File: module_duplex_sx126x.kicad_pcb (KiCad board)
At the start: 4 copper layers, 55.4 x 49.7 mm, 39 parts, among them J1 USB_B_Mini, J2 Conn_01x06_Pin, J3 Conn_01x05, J4 Conn_01x04, J6 Conn_01x02, SW1 SW_Push, U1 STM32F103C8Tx, U2 AMS1117-3.3, U3 SN65HVD230, U4 Ai-Thinker-Ra-02, U5 Ai-Thinker-Ra-02, Y1 16M, Y2 32.768k

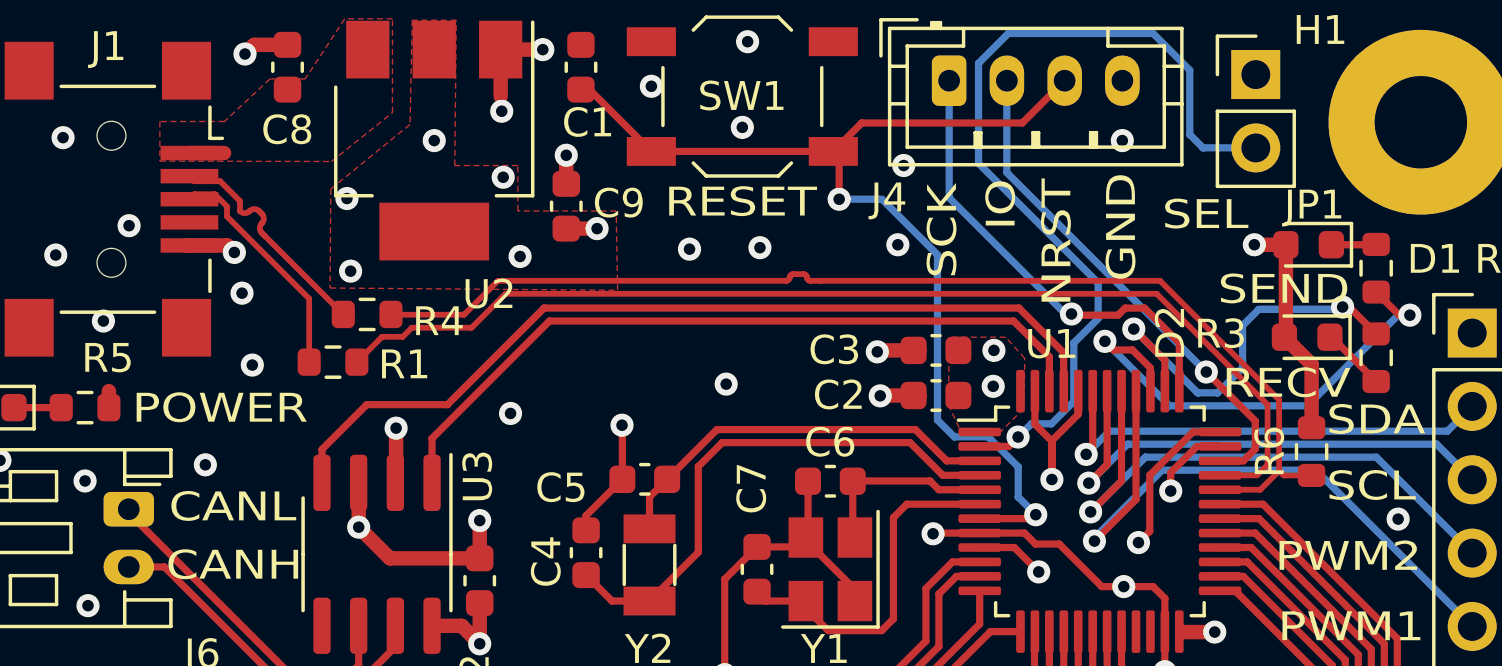
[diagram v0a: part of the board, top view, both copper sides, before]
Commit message: Moved pull up to correct USB_DP
Signed-off-by: Leonardo Celente <leocelente@gmail.com>
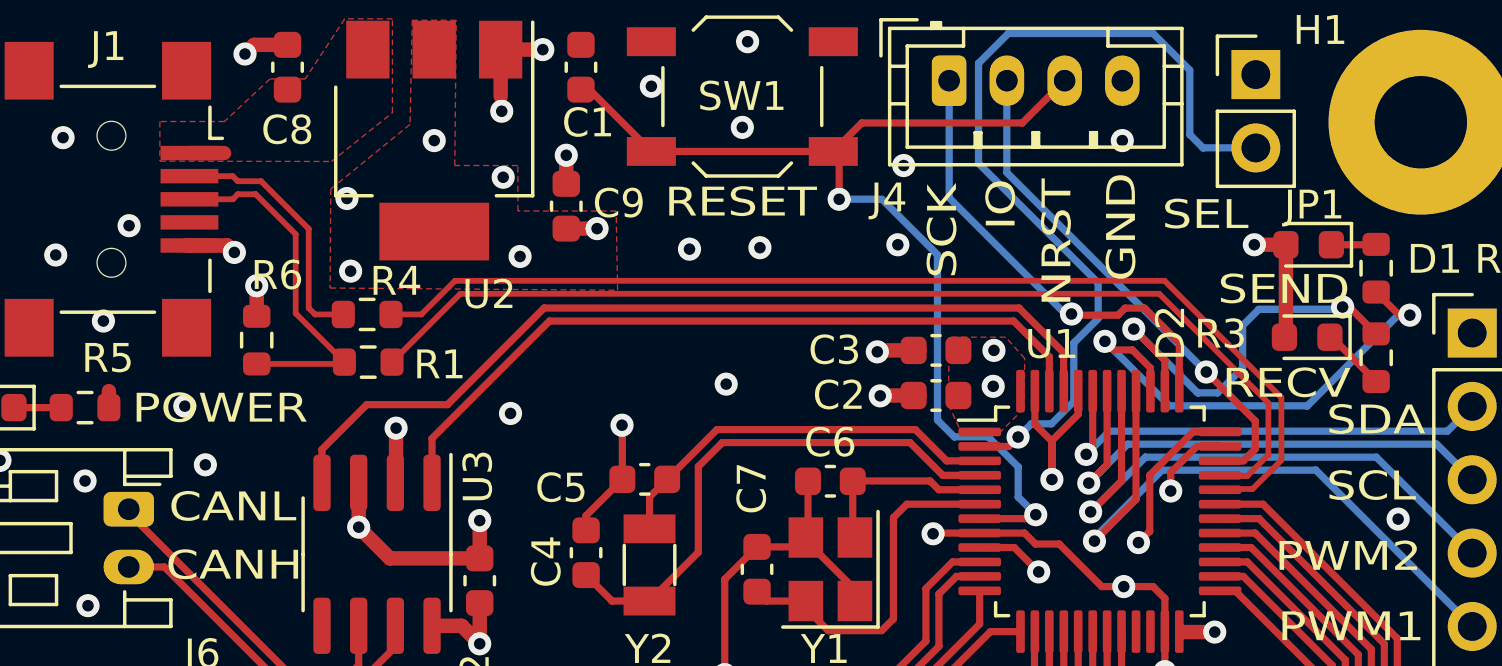
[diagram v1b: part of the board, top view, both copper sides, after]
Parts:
- moved R6 36.7 mm to (74.1, 56.2)
- moved R1 1.22 mm to (78.0, 56.9)
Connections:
- R6 pad 1: /USB_DN -> /CONN_DP
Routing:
- net /CONN_DP: track 8.12 -> 12.5 mm
- net VCC: track 50.8 -> 48.7 mm, vias 19 -> 20
- net /USB_DN: track 39.2 -> 37.7 mm
- net /USB_DP: track 38.0 -> 36.7 mm
- net /CONN_DN: track 8.01 -> 8.92 mm
- net GND: vias 85 -> 84

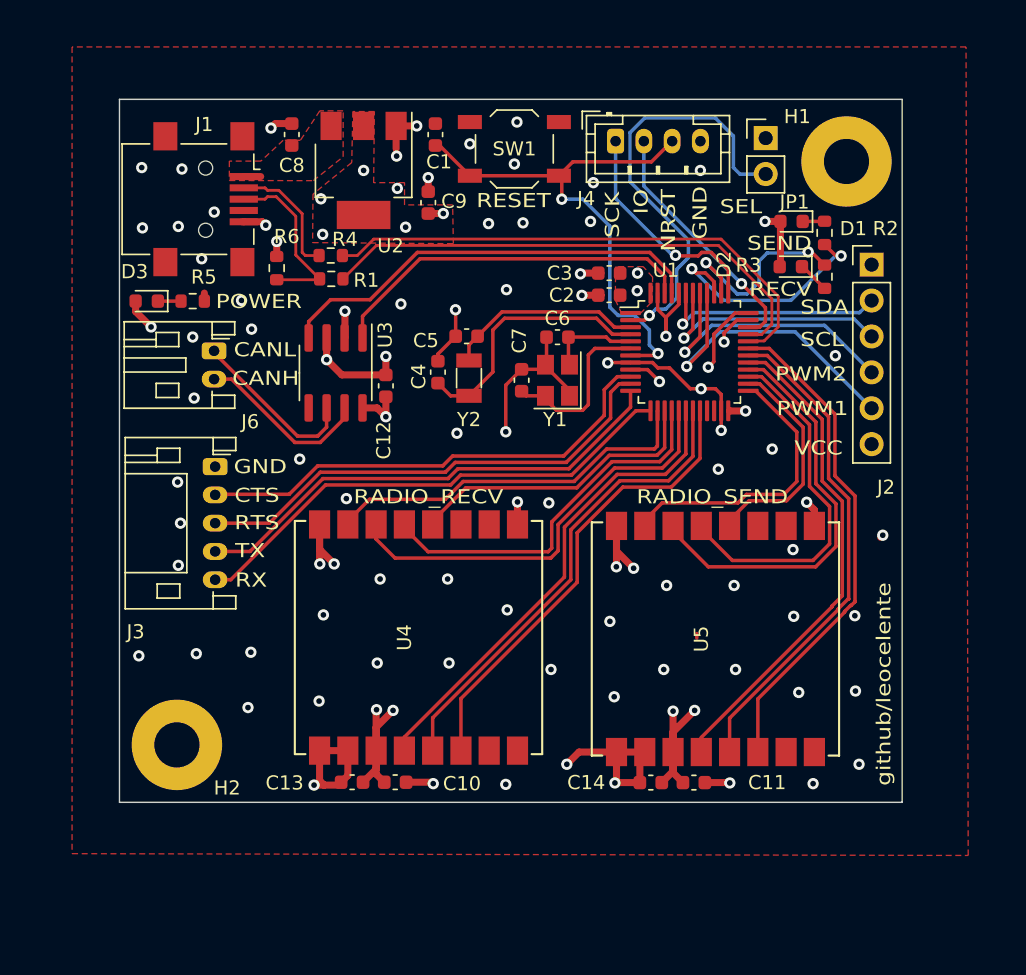
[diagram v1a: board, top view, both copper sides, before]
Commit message: Corrected DIO1 BUSY pin in radio module
Signed-off-by: Leonardo Celente <leocelente@gmail.com>
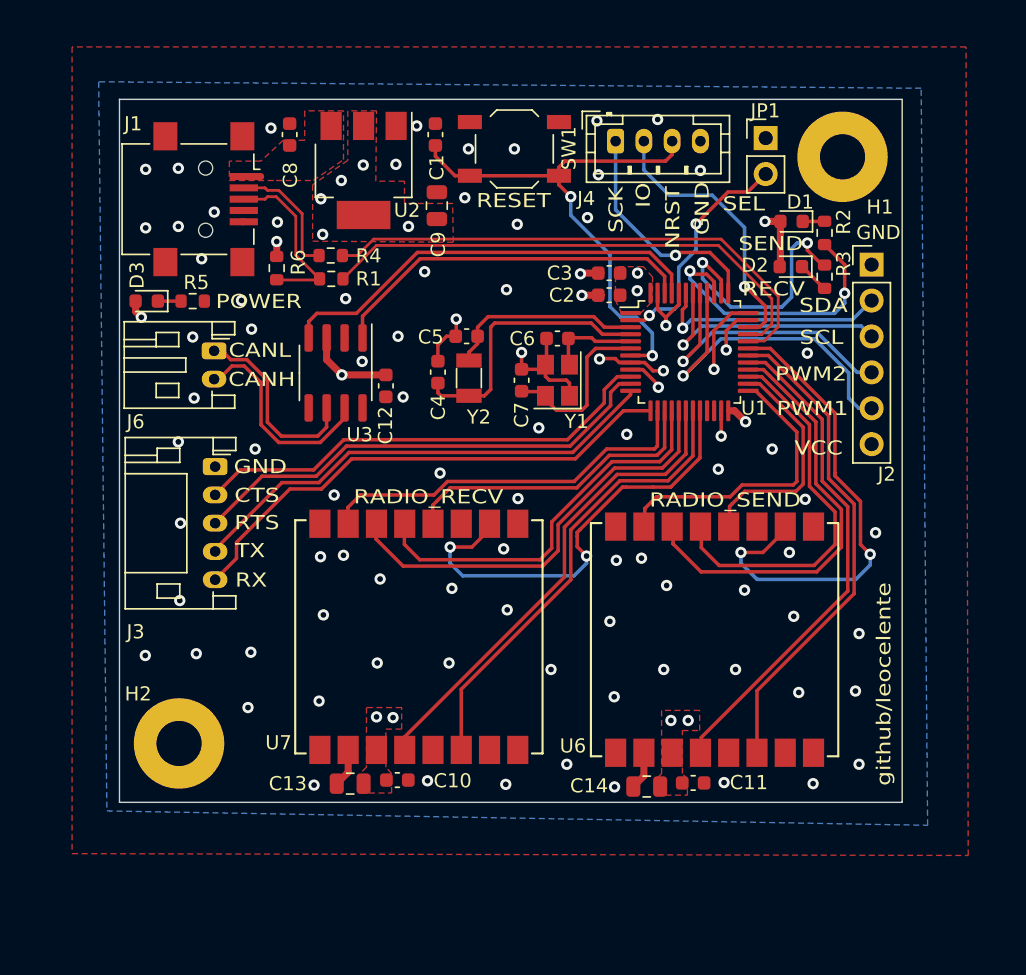
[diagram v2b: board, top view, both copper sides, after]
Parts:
- removed U4, U5: Ai-Thinker-Ra-02, RF_Module:Ai-Thinker-Ra-01-LoRa
- added U6: Ai-Thinker-Ra-01SH, RF_Module:Ai-Thinker-Ra-01-LoRa, F.Cu at (105.1, 82.5)
- added U7: Ai-Thinker-Ra-01SH, RF_Module:Ai-Thinker-Ra-01-LoRa, F.Cu at (84.2, 82.3)
- C13, C14, C9: value 4.7u -> 10u; footprint Capacitor_SMD:C_0603_1608Metric -> Capacitor_SMD:C_0805_2012Metric
- C8: value 4.7u -> 0.1u
- moved C9 0.65 mm to (85.4, 51.8)
- moved H1 0.43 mm to (114.1, 48.3)
- moved C14 0.40 mm to (100.3, 92.9)
- moved C10 0.22 mm to (82.7, 92.4)
- moved H2 0.18 mm to (67.2, 89.8)
- moved C13 0.17 mm to (79.3, 92.7)
- moved C8 0.15 mm to (75.0, 46.7)
- moved C6 0.09 mm to (94.0, 61.2)
- moved C11 0.06 mm to (103.6, 92.6)
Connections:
- U1 pad 19: /RADIO_RECV_DIO0 -> /RADIO_RECV_DIO1
- U1 pad 20: /RADIO_RECV_DIO1 -> /RADIO_RECV_BUSY
- U1 pad 30: /RADIO_SEND_DIO0 -> /RADIO_SEND_DIO1
- U1 pad 31: /RADIO_SEND_DIO1 -> /RADIO_SEND_BUSY
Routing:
- net GND: track 101.1 -> 41.3 mm, vias 84 -> 88
- net /RADIO_SEND_DIO0: track 35.3 -> 0.00 mm
- net /RADIO_SEND_BUSY: track 0.00 -> 34.7 mm, vias 0 -> 2
- net /RADIO_RECV_DIO0: track 33.7 -> 0.00 mm
- net /RADIO_RECV_BUSY: track 0.00 -> 31.9 mm, vias 0 -> 2
- net VCC: track 48.7 -> 22.7 mm, vias 20 -> 18
- net /SELECT: track 30.7 -> 16.5 mm, vias 1 -> 2
- net /RECV_LED: track 14.4 -> 18.2 mm
- net /SEND_LED: track 17.0 -> 20.4 mm
- net /CAN_H: track 12.5 -> 15.0 mm
- net /PWM_1: track 22.2 -> 24.1 mm
- net /SWDIO: track 17.7 -> 19.5 mm
- net /CAN_L: track 12.2 -> 13.8 mm
- net /RADIO_SEND_MISO: track 25.5 -> 27.1 mm
- net /RADIO_SEND_MOSI: track 29.3 -> 30.6 mm
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- added copper zone on B.Cu, net GND

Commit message: Added silkscreen diagram and symbols
Signed-off-by: Leonardo Celente <leocelente@gmail.com>
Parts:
- added G***: LOGO, 0_Diagram:diagram, B.Cu at (88.4, 58.1)
- added REF**: WEEE-Logo_4.2x6mm_SilkScreen, Symbol:WEEE-Logo_4.2x6mm_SilkScreen, B.Cu at (85.0, 76.7)
- added REF**: ESD-Logo_6.6x6mm_SilkScreen, Symbol:ESD-Logo_6.6x6mm_SilkScreen, B.Cu at (78.4, 76.6)
- added REF**: KiCad-Logo_5mm_SilkScreen, Symbol:KiCad-Logo_5mm_SilkScreen, B.Cu at (102.9, 76.0)
- added REF**: OSHW-Symbol_6.7x6mm_SilkScreen, Symbol:OSHW-Symbol_6.7x6mm_SilkScreen, B.Cu at (92.0, 76.7)
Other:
- board text added: "SWDCLK"
- board text added: "SWDIO"

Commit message: Updated Production and added README
Signed-off-by: Leonardo Celente <leocelente@gmail.com>
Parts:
- moved REF** 2.04 mm to (94.0, 76.6)
- moved REF** 1.79 mm to (104.7, 75.8)
- moved REF** 1.67 mm to (86.6, 76.9)
- moved REF** 1.05 mm to (79.4, 76.8)

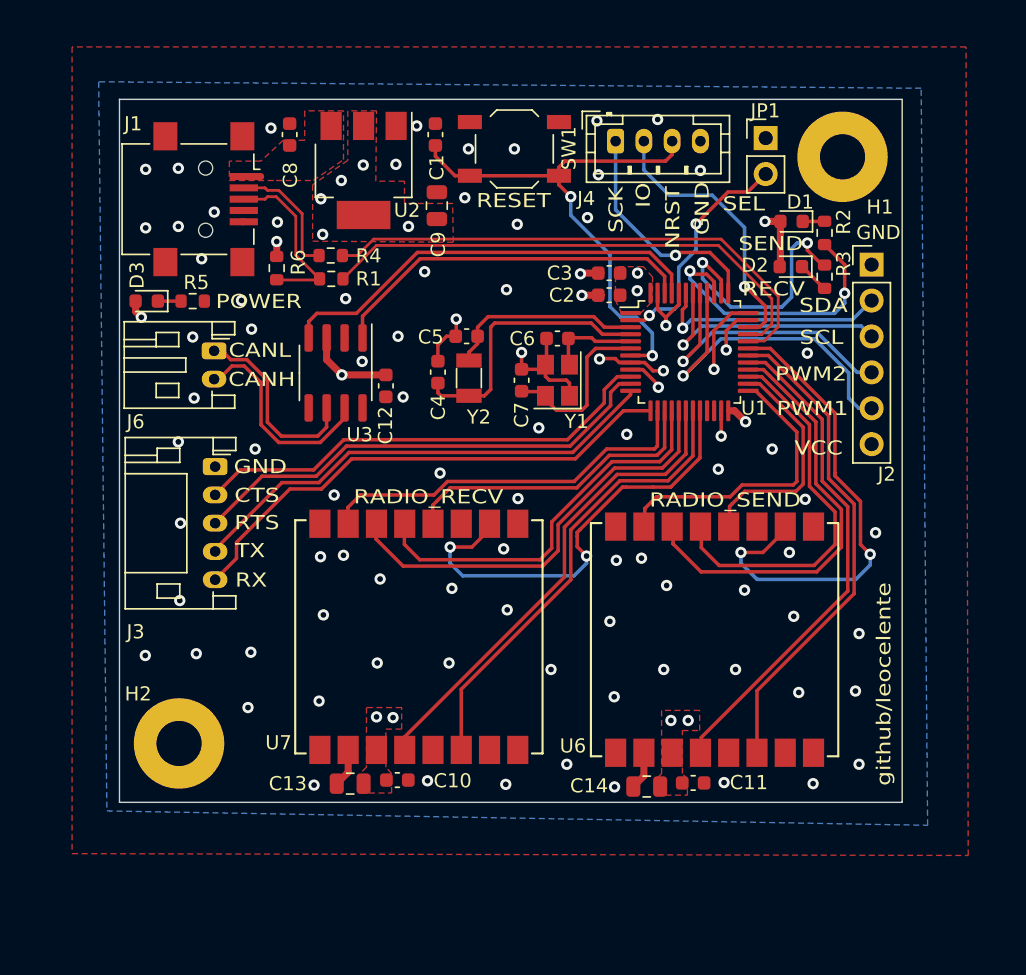
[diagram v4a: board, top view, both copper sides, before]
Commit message: Improved layout from Pudim's feedback
Signed-off-by: Leonardo Celente <leocelente@gmail.com>
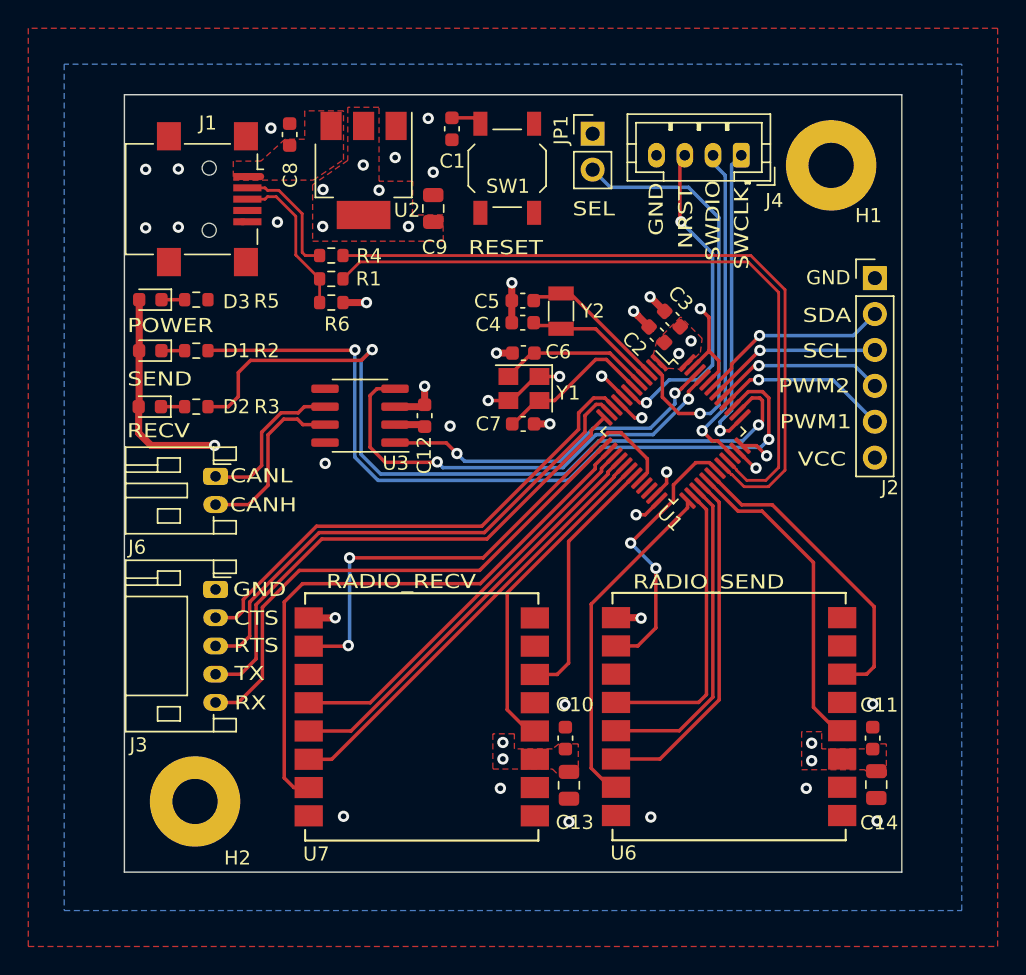
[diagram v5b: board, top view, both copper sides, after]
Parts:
- moved D2 46.4 mm to (65.1, 66.0)
- moved D1 46.3 mm to (65.2, 62.0)
- moved R3 45.4 mm to (68.4, 66.0), turned to 0 degrees
- moved R2 45.2 mm to (68.4, 62.0), turned to 0 degrees
- moved C14 16.2 mm to (116.5, 92.7), turned to -90 degrees
- moved C13 15.5 mm to (94.8, 92.8), turned to -90 degrees
- moved C11 13.1 mm to (116.3, 89.4), turned to 90 degrees
- moved C10 12.3 mm to (94.5, 89.4), turned to 90 degrees
- moved JP1 12.2 mm to (96.5, 46.7)
- moved J4 8.95 mm to (107.0, 48.2), turned to 180 degrees
- moved J6 8.88 mm to (69.8, 70.9)
- moved J3 8.69 mm to (69.8, 78.9)
- moved Y2 8.06 mm to (94.2, 59.2)
- moved C4 6.95 mm to (91.5, 60.0), turned to 0 degrees
- moved U1 5.74 mm to (102.2, 67.7), turned to -45 degrees
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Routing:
- net /RECV_LED: track 18.2 -> 56.3 mm
- net /SEND_LED: track 20.4 -> 55.3 mm
- net /RADIO_SEND_BUSY: track 34.7 -> 19.5 mm
- net /RADIO_RECV_DIO1: track 32.8 -> 17.9 mm
- net /RADIO_RECV_NSS: track 27.4 -> 42.1 mm
- net /SELECT: track 16.5 -> 30.6 mm, vias 2 -> 1
- net /RADIO_SEND_DIO1: track 34.9 -> 22.0 mm
- net /USB_DN: track 37.7 -> 50.6 mm
- net /RADIO_SEND_RST: track 35.5 -> 22.9 mm
- net /USB_DP: track 36.7 -> 49.2 mm
- net /NRST: track 37.7 -> 25.4 mm, vias 2 -> 3
- net /PWM_1: track 24.1 -> 12.3 mm
- net /RADIO_RECV_RST: track 34.3 -> 23.1 mm
- net /LSE_OUT: track 19.4 -> 9.43 mm
- net /PWM_2: track 20.7 -> 12.3 mm
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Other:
- board size 55.4 x 49.7 mm -> 55 x 55 mm
- board text added: "SWCLK"
- board text removed: "IO"
- board text removed: "SCK"
- board text removed: "github/leocelente"
